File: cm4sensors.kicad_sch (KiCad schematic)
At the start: 22 parts, among them J3 TSM-102-01-L-SV, J4 TSM-102-01-L-SV, U6 MCP9808T-E_MC, U7 ADS7142IRUGR, U8 MCP9808T-E_MC

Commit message: respin
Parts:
- renumbered C10 to C12, C11 to C13, C12 to C14, C13 to C15, C14 to C16, C15 to C17, C16 to C18, C17 to C19, R15 to R18, R16 to R19, R17 to R20, R18 to R21, R19 to R22, R20 to R23, R21 to R24, R22 to R25, R23 to R26, U6 to U7, U7 to U8, U8 to U9
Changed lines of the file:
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@@
   (symbol (lib_id "Device:C_Small") (at 137.795 147.32 0) (unit 1)
     (in_bom yes) (on_board yes) (fields_autoplaced)
-    (property "Reference" "C14" (id 0) (at 140.97 146.0562 0)
+    (property "Reference" "C16" (id 0) (at 140.97 146.0562 0)
       (effects (font (size 1.27 1.27)) (justify left))
     )
@@
   (symbol (lib_id "Sensor_I2C_Microchip:MCP9808T-E_MC") (at 215.265 85.09 0) (mirror y) (unit 1)
     (in_bom yes) (on_board yes)
-    (property "Reference" "U8" (id 0) (at 205.105 73.66 0)
+    (property "Reference" "U9" (id 0) (at 205.105 73.66 0)
       (effects (font (size 1.27 1.27)) (justify left))
     )
@@
   (symbol (lib_id "power:GND") (at 121.285 100.33 0) (unit 1)
     (in_bom yes) (on_board yes) (fields_autoplaced)
-    (property "Reference" "#PWR021" (id 0) (at 121.285 106.68 0)
+    (property "Reference" "#PWR022" (id 0) (at 121.285 106.68 0)
       (effects (font (size 1.27 1.27)) hide)
     )
@@
   (symbol (lib_id "Device:R_Small") (at 151.765 147.32 0) (unit 1)
     (in_bom yes) (on_board yes) (fields_autoplaced)
-    (property "Reference" "R19" (id 0) (at 153.67 146.0499 0)
+    (property "Reference" "R22" (id 0) (at 153.67 146.0499 0)
       (effects (font (size 1.27 1.27)) (justify left))
     )
@@
   (symbol (lib_id "power:GND") (at 197.485 101.6 0) (mirror y) (unit 1)
     (in_bom yes) (on_board yes)
-    (property "Reference" "#PWR024" (id 0) (at 197.485 107.95 0)
+    (property "Reference" "#PWR025" (id 0) (at 197.485 107.95 0)
       (effects (font (size 1.27 1.27)) hide)
     )
@@
   (symbol (lib_id "Device:C_Small") (at 51.435 68.58 0) (mirror y) (unit 1)
     (in_bom yes) (on_board yes) (fields_autoplaced)
-    (property "Reference" "C12" (id 0) (at 48.895 67.31 0)
+    (property "Reference" "C14" (id 0) (at 48.895 67.31 0)
       (effects (font (size 1.27 1.27)) (justify left))
     )
@@
   (symbol (lib_name "MCP9808T-E_MC_1") (lib_id "Sensor_I2C_Microchip:MCP9808T-E_MC") (at 84.455 83.82 0) (mirror y) (unit 1)
     (in_bom yes) (on_board yes)
-    (property "Reference" "U6" (id 0) (at 74.295 72.39 0)
+    (property "Reference" "U7" (id 0) (at 74.295 72.39 0)
       (effects (font (size 1.27 1.27)) (justify left))
     )
@@
   (symbol (lib_id "Analog_ADC_TI:ADS7142IRUGR") (at 107.95 149.225 0) (unit 1)
     (in_bom yes) (on_board yes)
-    (property "Reference" "U7" (id 0) (at 88.9 132.715 0)
+    (property "Reference" "U8" (id 0) (at 88.9 132.715 0)
       (effects (font (size 1.524 1.524)))
     )
@@
   (symbol (lib_id "Device:C_Small") (at 182.245 69.85 0) (mirror y) (unit 1)
     (in_bom yes) (on_board yes) (fields_autoplaced)
-    (property "Reference" "C17" (id 0) (at 179.705 68.58 0)
+    (property "Reference" "C19" (id 0) (at 179.705 68.58 0)
       (effects (font (size 1.27 1.27)) (justify left))
     )
@@
   (symbol (lib_id "power:GND") (at 40.005 76.2 0) (mirror y) (unit 1)
     (in_bom yes) (on_board yes)
-    (property "Reference" "#PWR018" (id 0) (at 40.005 82.55 0)
+    (property "Reference" "#PWR019" (id 0) (at 40.005 82.55 0)
       (effects (font (size 1.27 1.27)) hide)
     )
@@
   (symbol (lib_id "Device:R_Small") (at 245.745 90.17 90) (unit 1)
     (in_bom yes) (on_board yes)
-    (property "Reference" "R22" (id 0) (at 240.665 88.9 90))
+    (property "Reference" "R25" (id 0) (at 240.665 88.9 90))
     (property "Value" "1k" (id 1) (at 249.555 88.9 90))
     (property "Footprint" "Resistor_SMD:R_0402_1005Metric" (id 2) (at 245.745 90.17 0)
@@
   (symbol (lib_id "Device:R_Small") (at 245.745 92.71 90) (unit 1)
     (in_bom yes) (on_board yes)
-    (property "Reference" "R23" (id 0) (at 240.665 91.44 90))
+    (property "Reference" "R26" (id 0) (at 240.665 91.44 90))
     (property "Value" "1k" (id 1) (at 249.555 91.44 90))
     (property "Footprint" "Resistor_SMD:R_0402_1005Metric" (id 2) (at 245.745 92.71 0)
@@
   (symbol (lib_id "power:GND") (at 170.815 77.47 0) (mirror y) (unit 1)
     (in_bom yes) (on_board yes)
-    (property "Reference" "#PWR023" (id 0) (at 170.815 83.82 0)
+    (property "Reference" "#PWR024" (id 0) (at 170.815 83.82 0)
       (effects (font (size 1.27 1.27)) hide)
     )
@@
   (symbol (lib_id "Device:R_Small") (at 114.935 86.36 90) (unit 1)
     (in_bom yes) (on_board yes)
-    (property "Reference" "R16" (id 0) (at 109.855 85.09 90))
+    (property "Reference" "R19" (id 0) (at 109.855 85.09 90))
     (property "Value" "1k" (id 1) (at 118.745 85.09 90))
     (property "Footprint" "Resistor_SMD:R_0402_1005Metric" (id 2) (at 114.935 86.36 0)
@@
   (symbol (lib_id "power:GND") (at 252.095 101.6 0) (mirror y) (unit 1)
     (in_bom yes) (on_board yes)
-    (property "Reference" "#PWR025" (id 0) (at 252.095 107.95 0)
+    (property "Reference" "#PWR026" (id 0) (at 252.095 107.95 0)
       (effects (font (size 1.27 1.27)) hide)
     )
@@
   (symbol (lib_id "Device:C_Small") (at 137.795 167.64 0) (unit 1)
     (in_bom yes) (on_board yes) (fields_autoplaced)
-    (property "Reference" "C15" (id 0) (at 140.97 166.3762 0)
+    (property "Reference" "C17" (id 0) (at 140.97 166.3762 0)
       (effects (font (size 1.27 1.27)) (justify left))
     )
@@
   (symbol (lib_id "Device:C_Small") (at 48.26 137.16 0) (unit 1)
     (in_bom yes) (on_board yes) (fields_autoplaced)
-    (property "Reference" "C11" (id 0) (at 51.435 135.8962 0)
+    (property "Reference" "C13" (id 0) (at 51.435 135.8962 0)
       (effects (font (size 1.27 1.27)) (justify left))
     )
@@
   (symbol (lib_id "Device:R_Small") (at 245.745 87.63 90) (unit 1)
     (in_bom yes) (on_board yes)
-    (property "Reference" "R21" (id 0) (at 240.665 86.36 90))
+    (property "Reference" "R24" (id 0) (at 240.665 86.36 90))
     (property "Value" "1k" (id 1) (at 249.555 86.36 90))
     (property "Footprint" "Resistor_SMD:R_0402_1005Metric" (id 2) (at 245.745 87.63 0)
@@
   (symbol (lib_id "Device:R_Small") (at 151.765 167.64 0) (unit 1)
     (in_bom yes) (on_board yes) (fields_autoplaced)
-    (property "Reference" "R20" (id 0) (at 153.67 166.3699 0)
+    (property "Reference" "R23" (id 0) (at 153.67 166.3699 0)
       (effects (font (size 1.27 1.27)) (justify left))
     )
@@
   (symbol (lib_id "power:GND") (at 164.465 177.165 0) (unit 1)
     (in_bom yes) (on_board yes) (fields_autoplaced)
-    (property "Reference" "#PWR022" (id 0) (at 164.465 183.515 0)
+    (property "Reference" "#PWR023" (id 0) (at 164.465 183.515 0)
       (effects (font (size 1.27 1.27)) hide)
     )
@@
   (symbol (lib_id "Device:R_Small") (at 69.215 137.16 0) (unit 1)
     (in_bom yes) (on_board yes) (fields_autoplaced)
-    (property "Reference" "R15" (id 0) (at 71.12 135.8899 0)
+    (property "Reference" "R18" (id 0) (at 71.12 135.8899 0)
       (effects (font (size 1.27 1.27)) (justify left))
     )
@@
   (symbol (lib_id "power:GND") (at 48.26 177.165 0) (unit 1)
     (in_bom yes) (on_board yes) (fields_autoplaced)
-    (property "Reference" "#PWR019" (id 0) (at 48.26 183.515 0)
+    (property "Reference" "#PWR020" (id 0) (at 48.26 183.515 0)
       (effects (font (size 1.27 1.27)) hide)
     )
@@
   (symbol (lib_id "Device:R_Small") (at 114.935 91.44 90) (unit 1)
     (in_bom yes) (on_board yes)
-    (property "Reference" "R18" (id 0) (at 109.855 90.17 90))
+    (property "Reference" "R21" (id 0) (at 109.855 90.17 90))
     (property "Value" "1k" (id 1) (at 118.745 90.17 90))
     (property "Footprint" "Resistor_SMD:R_0402_1005Metric" (id 2) (at 114.935 91.44 0)
@@
   (symbol (lib_id "Device:C_Small") (at 40.005 68.58 0) (mirror y) (unit 1)
     (in_bom yes) (on_board yes) (fields_autoplaced)
-    (property "Reference" "C10" (id 0) (at 37.465 67.31 0)
+    (property "Reference" "C12" (id 0) (at 37.465 67.31 0)
       (effects (font (size 1.27 1.27)) (justify left))
     )
@@
   (symbol (lib_id "Device:C_Small") (at 170.815 69.85 0) (mirror y) (unit 1)
     (in_bom yes) (on_board yes) (fields_autoplaced)
-    (property "Reference" "C16" (id 0) (at 168.275 68.58 0)
+    (property "Reference" "C18" (id 0) (at 168.275 68.58 0)
       (effects (font (size 1.27 1.27)) (justify left))
     )
@@
   (symbol (lib_id "Device:C_Small") (at 58.42 137.16 0) (unit 1)
     (in_bom yes) (on_board yes) (fields_autoplaced)
-    (property "Reference" "C13" (id 0) (at 61.595 135.8962 0)
+    (property "Reference" "C15" (id 0) (at 61.595 135.8962 0)
       (effects (font (size 1.27 1.27)) (justify left))
     )
@@
   (symbol (lib_id "power:GND") (at 66.675 100.33 0) (unit 1)
     (in_bom yes) (on_board yes) (fields_autoplaced)
-    (property "Reference" "#PWR020" (id 0) (at 66.675 106.68 0)
+    (property "Reference" "#PWR021" (id 0) (at 66.675 106.68 0)
       (effects (font (size 1.27 1.27)) hide)
     )
@@
   (symbol (lib_id "Device:R_Small") (at 114.935 88.9 90) (unit 1)
     (in_bom yes) (on_board yes)
-    (property "Reference" "R17" (id 0) (at 109.855 87.63 90))
+    (property "Reference" "R20" (id 0) (at 109.855 87.63 90))
     (property "Value" "1k" (id 1) (at 118.745 87.63 90))
     (property "Footprint" "Resistor_SMD:R_0402_1005Metric" (id 2) (at 114.935 88.9 0)

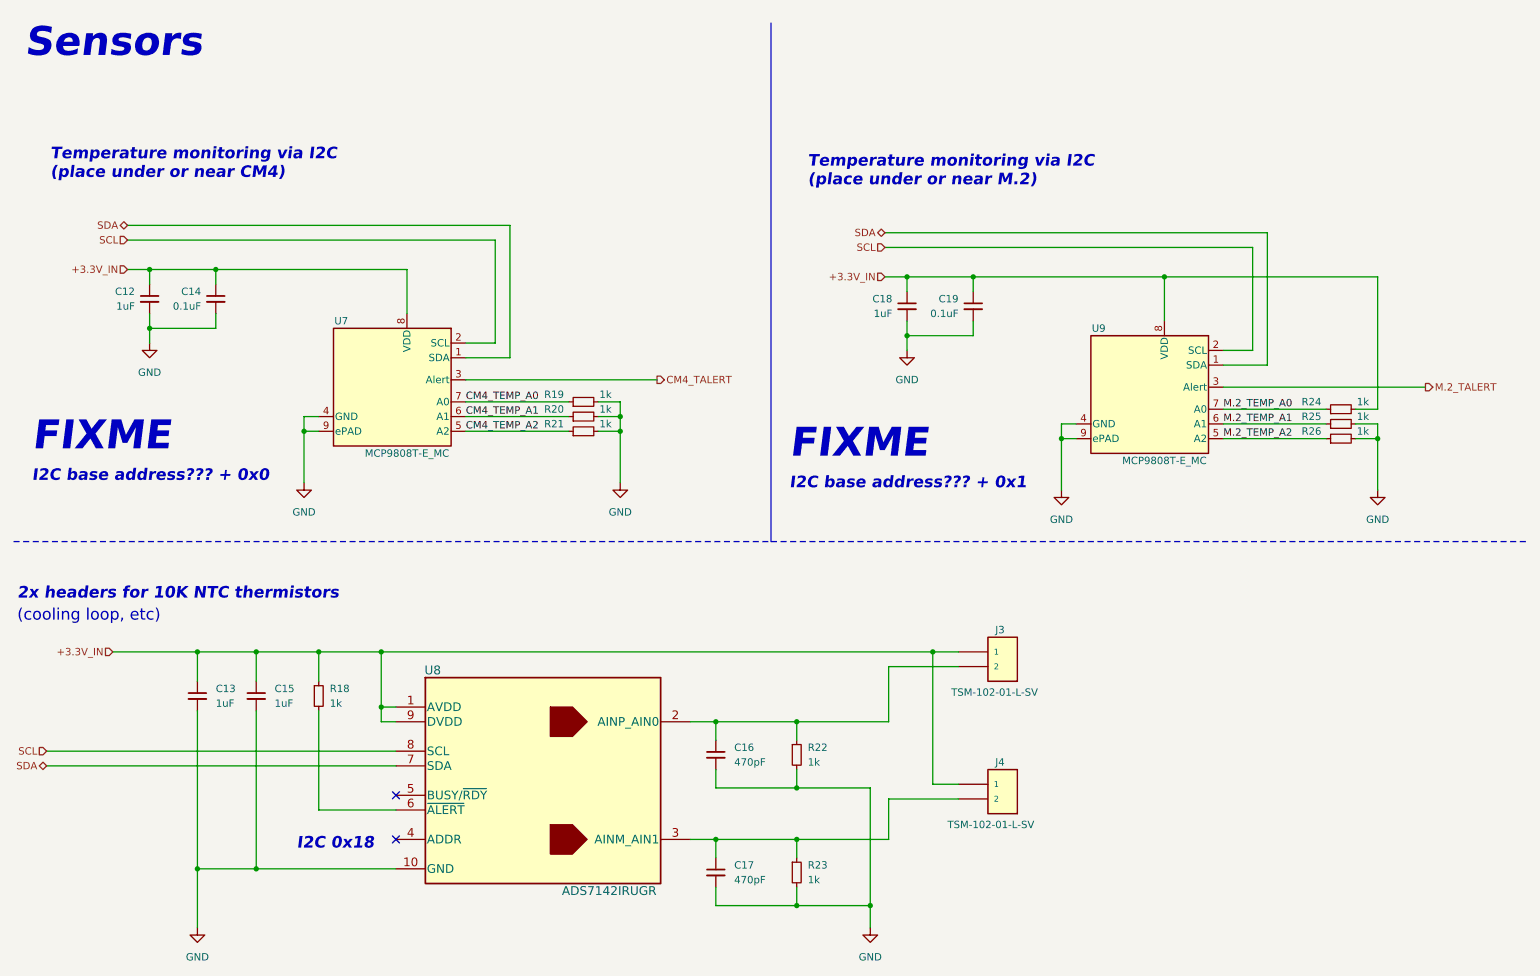
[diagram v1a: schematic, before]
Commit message: fixed I2C ping indicator
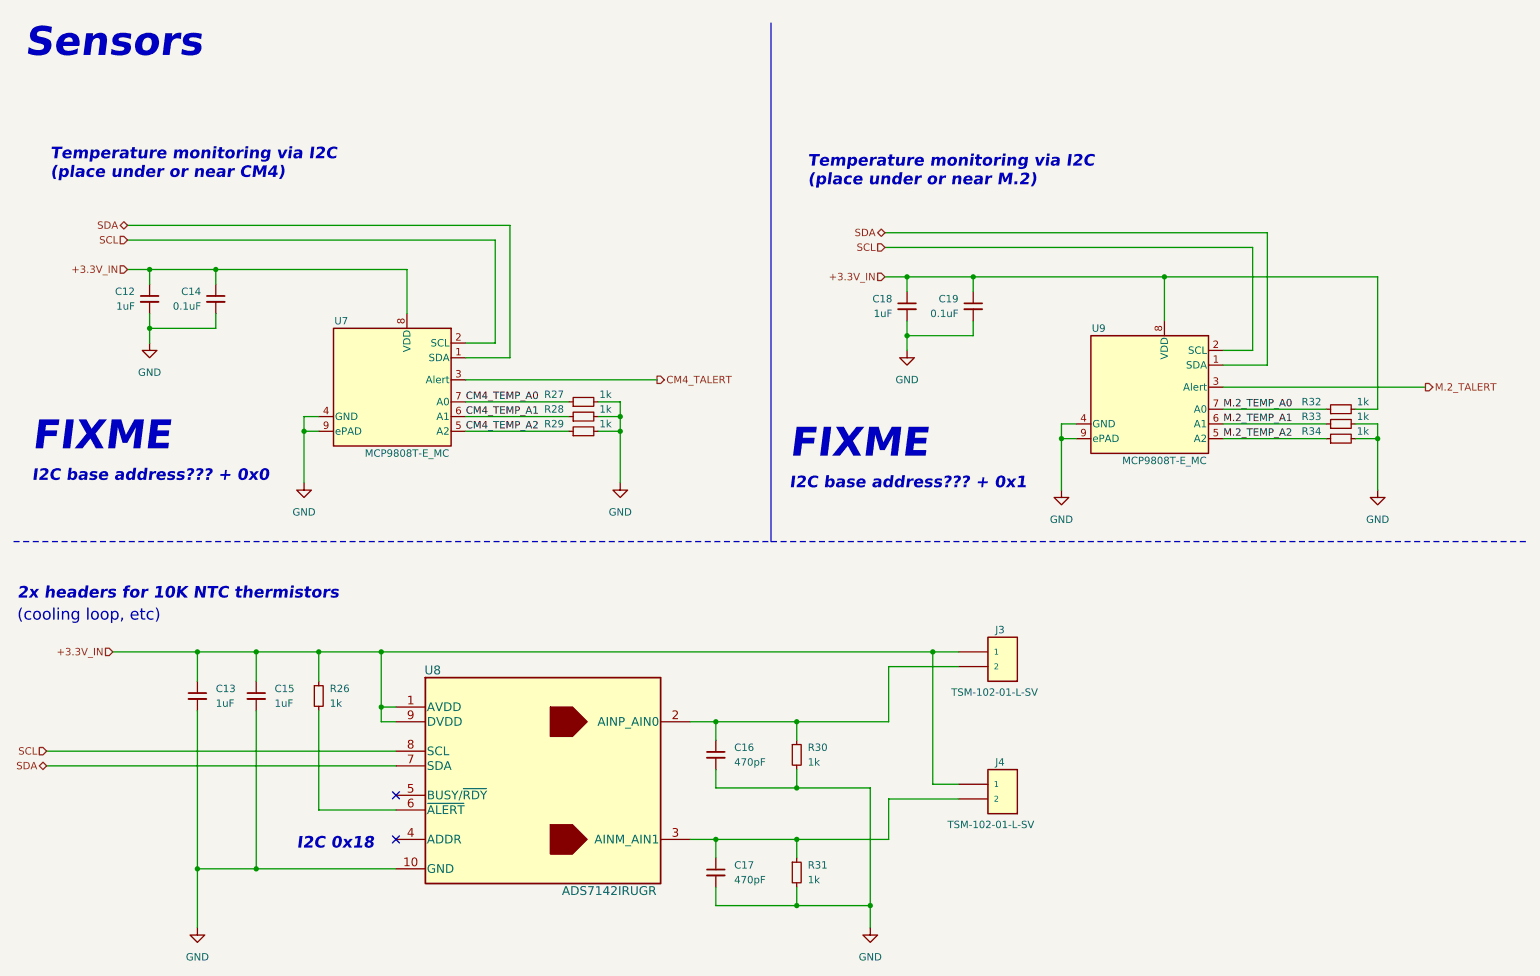
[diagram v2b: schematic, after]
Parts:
- renumbered R18 to R26, R19 to R27, R20 to R28, R21 to R29, R22 to R30, R23 to R31, R24 to R32, R25 to R33, R26 to R34
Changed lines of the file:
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@@
   (symbol (lib_id "power:GND") (at 121.285 100.33 0) (unit 1)
     (in_bom yes) (on_board yes) (fields_autoplaced)
-    (property "Reference" "#PWR022" (id 0) (at 121.285 106.68 0)
+    (property "Reference" "#PWR024" (id 0) (at 121.285 106.68 0)
       (effects (font (size 1.27 1.27)) hide)
     )
@@
   (symbol (lib_id "Device:R_Small") (at 151.765 147.32 0) (unit 1)
     (in_bom yes) (on_board yes) (fields_autoplaced)
-    (property "Reference" "R22" (id 0) (at 153.67 146.0499 0)
+    (property "Reference" "R30" (id 0) (at 153.67 146.0499 0)
       (effects (font (size 1.27 1.27)) (justify left))
     )
@@
   (symbol (lib_id "power:GND") (at 197.485 101.6 0) (mirror y) (unit 1)
     (in_bom yes) (on_board yes)
-    (property "Reference" "#PWR025" (id 0) (at 197.485 107.95 0)
+    (property "Reference" "#PWR027" (id 0) (at 197.485 107.95 0)
       (effects (font (size 1.27 1.27)) hide)
     )
@@
   (symbol (lib_id "power:GND") (at 40.005 76.2 0) (mirror y) (unit 1)
     (in_bom yes) (on_board yes)
-    (property "Reference" "#PWR019" (id 0) (at 40.005 82.55 0)
+    (property "Reference" "#PWR021" (id 0) (at 40.005 82.55 0)
       (effects (font (size 1.27 1.27)) hide)
     )
@@
   (symbol (lib_id "Device:R_Small") (at 245.745 90.17 90) (unit 1)
     (in_bom yes) (on_board yes)
-    (property "Reference" "R25" (id 0) (at 240.665 88.9 90))
+    (property "Reference" "R33" (id 0) (at 240.665 88.9 90))
     (property "Value" "1k" (id 1) (at 249.555 88.9 90))
     (property "Footprint" "Resistor_SMD:R_0402_1005Metric" (id 2) (at 245.745 90.17 0)
@@
   (symbol (lib_id "Device:R_Small") (at 245.745 92.71 90) (unit 1)
     (in_bom yes) (on_board yes)
-    (property "Reference" "R26" (id 0) (at 240.665 91.44 90))
+    (property "Reference" "R34" (id 0) (at 240.665 91.44 90))
     (property "Value" "1k" (id 1) (at 249.555 91.44 90))
     (property "Footprint" "Resistor_SMD:R_0402_1005Metric" (id 2) (at 245.745 92.71 0)
@@
   (symbol (lib_id "power:GND") (at 170.815 77.47 0) (mirror y) (unit 1)
     (in_bom yes) (on_board yes)
-    (property "Reference" "#PWR024" (id 0) (at 170.815 83.82 0)
+    (property "Reference" "#PWR026" (id 0) (at 170.815 83.82 0)
       (effects (font (size 1.27 1.27)) hide)
     )
@@
   (symbol (lib_id "Device:R_Small") (at 114.935 86.36 90) (unit 1)
     (in_bom yes) (on_board yes)
-    (property "Reference" "R19" (id 0) (at 109.855 85.09 90))
+    (property "Reference" "R27" (id 0) (at 109.855 85.09 90))
     (property "Value" "1k" (id 1) (at 118.745 85.09 90))
     (property "Footprint" "Resistor_SMD:R_0402_1005Metric" (id 2) (at 114.935 86.36 0)
@@
   (symbol (lib_id "power:GND") (at 252.095 101.6 0) (mirror y) (unit 1)
     (in_bom yes) (on_board yes)
-    (property "Reference" "#PWR026" (id 0) (at 252.095 107.95 0)
+    (property "Reference" "#PWR028" (id 0) (at 252.095 107.95 0)
       (effects (font (size 1.27 1.27)) hide)
     )
@@
   (symbol (lib_id "Device:R_Small") (at 245.745 87.63 90) (unit 1)
     (in_bom yes) (on_board yes)
-    (property "Reference" "R24" (id 0) (at 240.665 86.36 90))
+    (property "Reference" "R32" (id 0) (at 240.665 86.36 90))
     (property "Value" "1k" (id 1) (at 249.555 86.36 90))
     (property "Footprint" "Resistor_SMD:R_0402_1005Metric" (id 2) (at 245.745 87.63 0)
@@
   (symbol (lib_id "Device:R_Small") (at 151.765 167.64 0) (unit 1)
     (in_bom yes) (on_board yes) (fields_autoplaced)
-    (property "Reference" "R23" (id 0) (at 153.67 166.3699 0)
+    (property "Reference" "R31" (id 0) (at 153.67 166.3699 0)
       (effects (font (size 1.27 1.27)) (justify left))
     )
@@
   (symbol (lib_id "power:GND") (at 164.465 177.165 0) (unit 1)
     (in_bom yes) (on_board yes) (fields_autoplaced)
-    (property "Reference" "#PWR023" (id 0) (at 164.465 183.515 0)
+    (property "Reference" "#PWR025" (id 0) (at 164.465 183.515 0)
       (effects (font (size 1.27 1.27)) hide)
     )
@@
   (symbol (lib_id "Device:R_Small") (at 69.215 137.16 0) (unit 1)
     (in_bom yes) (on_board yes) (fields_autoplaced)
-    (property "Reference" "R18" (id 0) (at 71.12 135.8899 0)
+    (property "Reference" "R26" (id 0) (at 71.12 135.8899 0)
       (effects (font (size 1.27 1.27)) (justify left))
     )
@@
   (symbol (lib_id "power:GND") (at 48.26 177.165 0) (unit 1)
     (in_bom yes) (on_board yes) (fields_autoplaced)
-    (property "Reference" "#PWR020" (id 0) (at 48.26 183.515 0)
+    (property "Reference" "#PWR022" (id 0) (at 48.26 183.515 0)
       (effects (font (size 1.27 1.27)) hide)
     )
@@
   (symbol (lib_id "Device:R_Small") (at 114.935 91.44 90) (unit 1)
     (in_bom yes) (on_board yes)
-    (property "Reference" "R21" (id 0) (at 109.855 90.17 90))
+    (property "Reference" "R29" (id 0) (at 109.855 90.17 90))
     (property "Value" "1k" (id 1) (at 118.745 90.17 90))
     (property "Footprint" "Resistor_SMD:R_0402_1005Metric" (id 2) (at 114.935 91.44 0)
@@
   (symbol (lib_id "power:GND") (at 66.675 100.33 0) (unit 1)
     (in_bom yes) (on_board yes) (fields_autoplaced)
-    (property "Reference" "#PWR021" (id 0) (at 66.675 106.68 0)
+    (property "Reference" "#PWR023" (id 0) (at 66.675 106.68 0)
       (effects (font (size 1.27 1.27)) hide)
     )
@@
   (symbol (lib_id "Device:R_Small") (at 114.935 88.9 90) (unit 1)
     (in_bom yes) (on_board yes)
-    (property "Reference" "R20" (id 0) (at 109.855 87.63 90))
+    (property "Reference" "R28" (id 0) (at 109.855 87.63 90))
     (property "Value" "1k" (id 1) (at 118.745 87.63 90))
     (property "Footprint" "Resistor_SMD:R_0402_1005Metric" (id 2) (at 114.935 88.9 0)
